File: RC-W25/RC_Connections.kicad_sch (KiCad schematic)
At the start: 23 parts, among them J1 USB_C_Receptacle_USB2.0_14P, U1 ESP32-C6-WROOM-1, U2 AP62300TWU

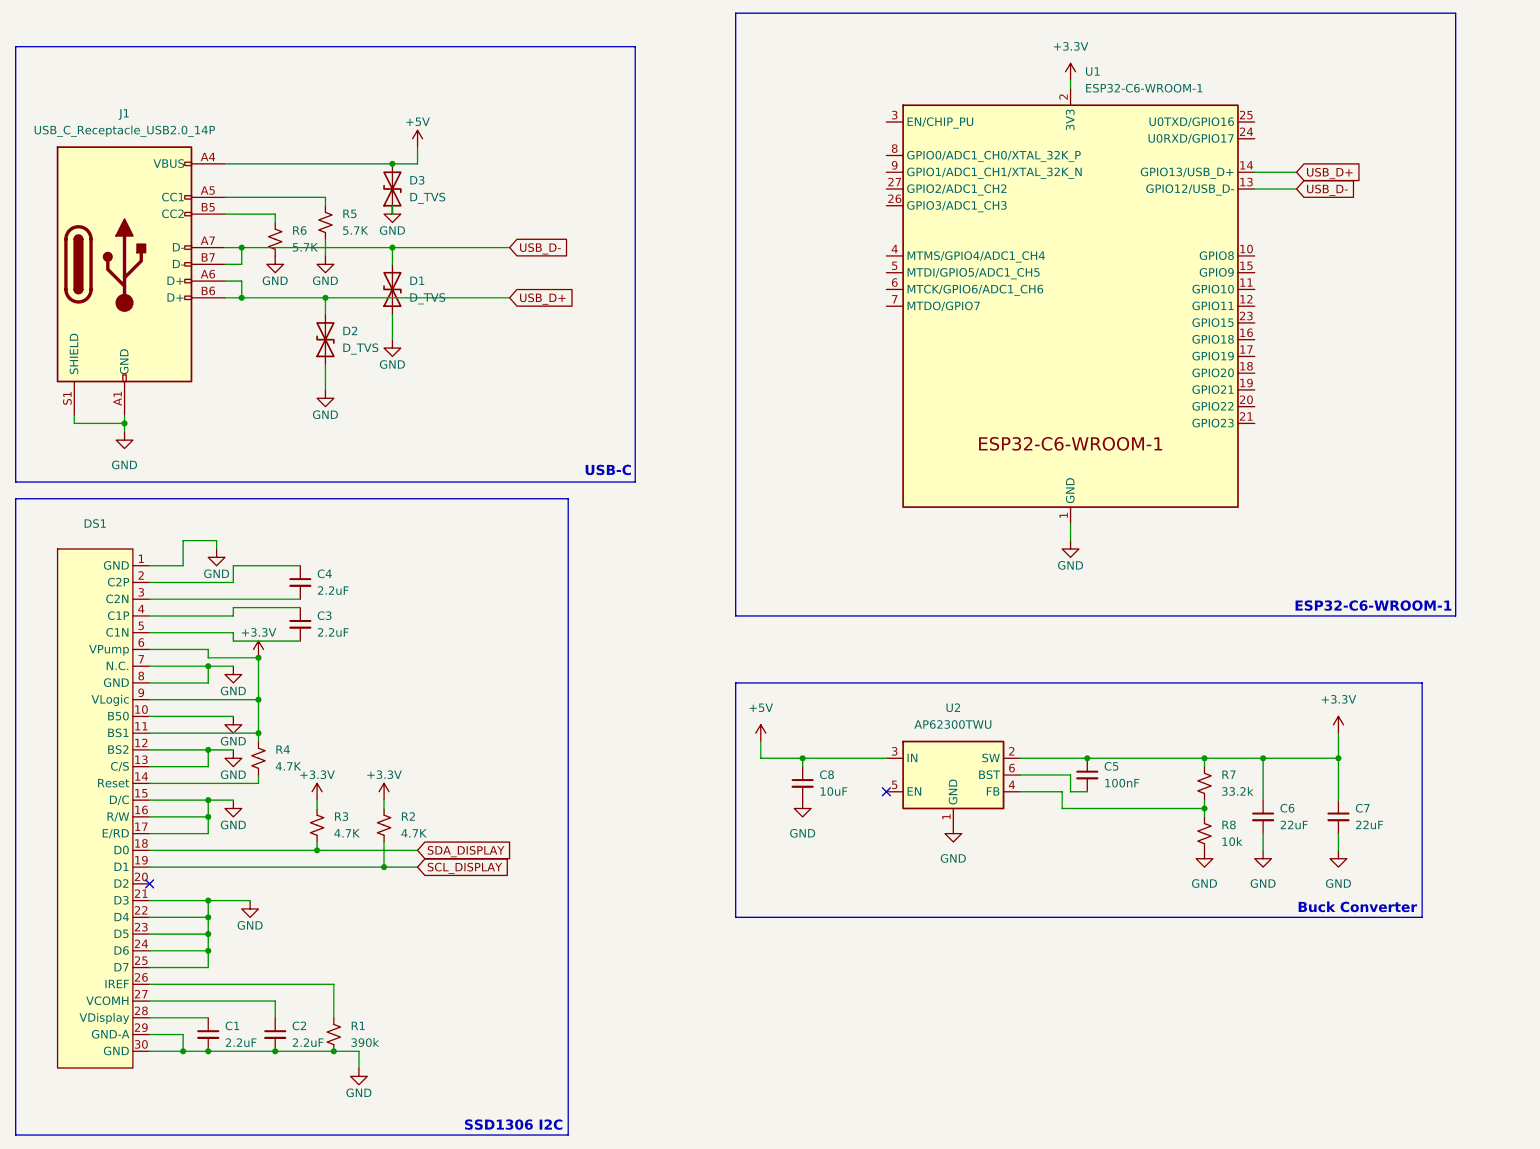
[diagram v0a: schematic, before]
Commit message: Schematic Update
Added buttons with debouncing and DC motor duraclik connector
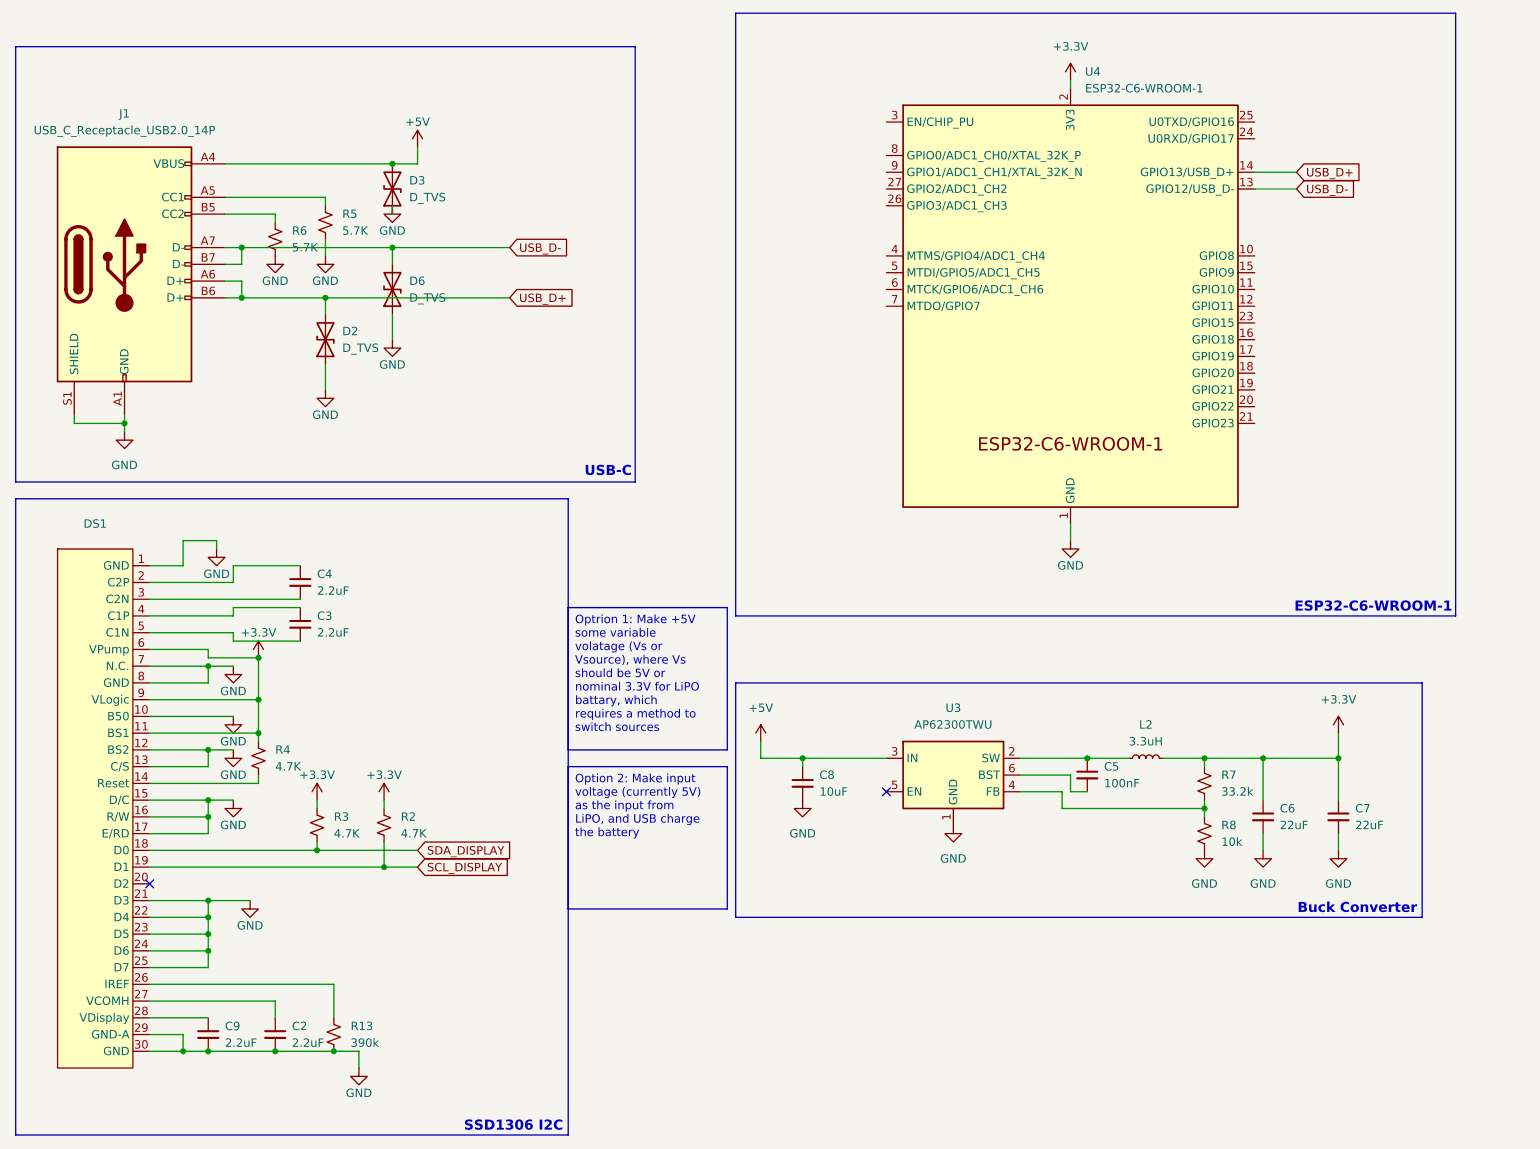
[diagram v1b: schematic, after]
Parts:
- added L2: 3.3uH, symbol Device:L_Small
- renumbered C1 to C9, D1 to D6, R1 to R13, U2 to U3, U1 to U4
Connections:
- net +3.3V: now also L2.2; no longer C5.1, U3.2 (SW)
- new net: C5.1, L2.1, U3.2 (SW)
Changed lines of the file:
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@@
 	(wire
 		(pts
+			(xy 207.01 133.35) (xy 213.36 133.35)
+		)
+		(stroke
+			(width 0)
+			(type default)
+		)
+	)
+	(wire
+		(pts
 			(xy 66.04 106.68) (xy 66.04 104.14)
 		)
@@
 	(wire
 		(pts
-			(xy 195.58 133.35) (xy 213.36 133.35)
+			(xy 195.58 133.35) (xy 201.93 133.35)
 		)
 		(stroke
@@
 		)
 	)
+	(text_box "Optrion 1: Make +5V some variable volatage (Vs or Vsource), where Vs should be 5V or nominal 3.3V for LiPO battary, which requires a method to switch sources"
+		(exclude_from_sim no)
+		(at 116.84 110.49 0)
+		(size 24.13 21.59)
+		(stroke
+			(width 0)
+			(type default)
+		)
+		(fill
+			(type none)
+		)
+		(effects
+			(font
+				(size 1.27 1.27)
+			)
+			(justify left top)
+		)
+	)
+	(text_box "Option 2: Make input voltage (currently 5V) as the input from LiPO, and USB charge the battery"
+		(exclude_from_sim no)
+		(at 116.84 134.62 0)
+		(size 24.13 21.59)
+		(stroke
+			(width 0)
+			(type default)
+		)
+		(fill
+			(type none)
+		)
+		(effects
+			(font
+				(size 1.27 1.27)
+			)
+			(justify left top)
+		)
+	)
 	(text "USB-C"
 		(exclude_from_sim no)
@@
 		(on_board yes)
 		(dnp no)
-		(property "Reference" "#PWR04"
+		(property "Reference" "#PWR036"
 			(at 78.74 143.51 0)
 			(effects
@@
 		(pin "1"
 		)
-		(instances
-			(project ""
-				(path "/427b2895-e3a6-4096-b101-5f65a3f7473e/01bd870e-4674-4257-9660-564635d632de"
-					(reference "#PWR04")
-					(unit 1)
-				)
-			)
-		)
 	)
 	(symbol
@@
 		(dnp no)
 		(fields_autoplaced yes)
-		(property "Reference" "U2"
+		(property "Reference" "U3"
 			(at 175.26 125.73 0)
 			(effects
@@
 		(pin "2"
 		)
-		(instances
-			(project ""
-				(path "/427b2895-e3a6-4096-b101-5f65a3f7473e/01bd870e-4674-4257-9660-564635d632de"
-					(reference "U2")
-					(unit 1)
-				)
-			)
-		)
 	)
 	(symbol
@@
 		(dnp no)
 		(fields_autoplaced yes)
-		(property "Reference" "#PWR021"
+		(property "Reference" "#PWR051"
 			(at 233.68 133.35 0)
 			(effects
@@
 		(pin "1"
 		)
-		(instances
-			(project ""
-				(path "/427b2895-e3a6-4096-b101-5f65a3f7473e/01bd870e-4674-4257-9660-564635d632de"
-					(reference "#PWR021")
-					(unit 1)
-				)
-			)
-		)
 	)
 	(symbol
@@
 		(on_board yes)
 		(dnp no)
-		(property "Reference" "#PWR026"
+		(property "Reference" "#PWR045"
 			(at 152.4 146.05 0)
 			(effects
@@
 		(pin "1"
 		)
-		(instances
-			(project ""
-				(path "/427b2895-e3a6-4096-b101-5f65a3f7473e/01bd870e-4674-4257-9660-564635d632de"
-					(reference "#PWR026")
-					(unit 1)
-				)
-			)
-		)
 	)
 	(symbol
@@
 		(dnp no)
 		(fields_autoplaced yes)
-		(property "Reference" "D1"
+		(property "Reference" "D6"
 			(at 92.71 60.9599 90)
 			(effects
@@
 		(pin "2"
 		)
-		(instances
-			(project ""
-				(path "/427b2895-e3a6-4096-b101-5f65a3f7473e/01bd870e-4674-4257-9660-564635d632de"
-					(reference "D1")
-					(unit 1)
-				)
-			)
-		)
 	)
 	(symbol
@@
 		(on_board yes)
 		(dnp no)
-		(property "Reference" "#PWR03"
+		(property "Reference" "#PWR033"
 			(at 68.58 161.29 0)
 			(effects
@@
 		(pin "1"
 		)
-		(instances
-			(project ""
-				(path "/427b2895-e3a6-4096-b101-5f65a3f7473e/01bd870e-4674-4257-9660-564635d632de"
-					(reference "#PWR03")
-					(unit 1)
-				)
-			)
-		)
 	)
 	(symbol
@@
 		(on_board yes)
 		(dnp no)
-		(property "Reference" "#PWR015"
+		(property "Reference" "#PWR043"
 			(at 93.98 44.45 0)
 			(effects
@@
 		(pin "1"
 		)
-		(instances
-			(project ""
-				(path "/427b2895-e3a6-4096-b101-5f65a3f7473e/01bd870e-4674-4257-9660-564635d632de"
-					(reference "#PWR015")
-					(unit 1)
-				)
-			)
-		)
 	)
 	(symbol
@@
 		(dnp no)
 		(fields_autoplaced yes)
-		(property "Reference" "#PWR020"
+		(property "Reference" "#PWR046"
 			(at 175.26 149.86 0)
 			(effects
@@
 		(pin "1"
 		)
-		(instances
-			(project ""
-				(path "/427b2895-e3a6-4096-b101-5f65a3f7473e/01bd870e-4674-4257-9660-564635d632de"
-					(reference "#PWR020")
-					(unit 1)
-				)
-			)
-		)
 	)
 	(symbol
@@
 		(dnp no)
 		(fields_autoplaced yes)
-		(property "Reference" "U1"
+		(property "Reference" "U4"
 			(at 195.2341 29.21 0)
 			(effects
@@
 		(pin "9"
 		)
-		(instances
-			(project ""
-				(path "/427b2895-e3a6-4096-b101-5f65a3f7473e/01bd870e-4674-4257-9660-564635d632de"
-					(reference "U1")
-					(unit 1)
-				)
-			)
-		)
 	)
 	(symbol
@@
 		(dnp no)
 		(fields_autoplaced yes)
-		(property "Reference" "R1"
+		(property "Reference" "R13"
 			(at 83.82 173.9899 0)
 			(effects
@@
 		(pin "2"
 		)
-		(instances
-			(project ""
-				(path "/427b2895-e3a6-4096-b101-5f65a3f7473e/01bd870e-4674-4257-9660-564635d632de"
-					(reference "R1")
-					(unit 1)
-				)
-			)
-		)
 	)
 	(symbol
@@
 		(dnp no)
 		(fields_autoplaced yes)
-		(property "Reference" "#PWR025"
+		(property "Reference" "#PWR044"
 			(at 146.05 134.62 0)
 			(effects
@@
 		(pin "1"
 		)
-		(instances
-			(project ""
-				(path "/427b2895-e3a6-4096-b101-5f65a3f7473e/01bd870e-4674-4257-9660-564635d632de"
-					(reference "#PWR025")
-					(unit 1)
-				)
-			)
-		)
 	)
 	(symbol
@@
 		(dnp no)
 		(fields_autoplaced yes)
-		(property "Reference" "#PWR019"
+		(property "Reference" "#PWR047"
 			(at 193.04 34.29 0)
 			(effects
@@
 		(pin "1"
 		)
-		(instances
-			(project ""
-				(path "/427b2895-e3a6-4096-b101-5f65a3f7473e/01bd870e-4674-4257-9660-564635d632de"
-					(reference "#PWR019")
-					(unit 1)
-				)
-			)
-		)
 	)
 	(symbol
@@
 	)
 	(symbol
+		(lib_id "Device:L_Small")
+		(at 204.47 133.35 90)
+		(unit 1)
+		(exclude_from_sim no)
+		(in_bom yes)
+		(on_board yes)
+		(dnp no)
+		(fields_autoplaced yes)
+		(property "Reference" "L2"
+			(at 204.47 128.27 90)
+			(effects
+				(font
+					(size 1.27 1.27)
+				)
+			)
+		)
+		(property "Value" "3.3uH"
+			(at 204.47 130.81 90)
+			(effects
+				(font
+					(size 1.27 1.27)
+				)
+			)
+		)
+		(property "Footprint" ""
+			(at 204.47 133.35 0)
+			(effects
+				(font
+					(size 1.27 1.27)
+				)
+				(hide yes)
+			)
+		)
+		(property "Datasheet" "~"
+			(at 204.47 133.35 0)
+			(effects
+				(font
+					(size 1.27 1.27)
+				)
+				(hide yes)
+			)
+		)
+		(property "Description" "Inductor, small symbol"
+			(at 204.47 133.35 0)
+			(effects
+				(font
+					(size 1.27 1.27)
+				)
+				(hide yes)
+			)
+		)
+		(pin "1"
+		)
+		(pin "2"
+		)
+	)
+	(symbol
 		(lib_id "power:GND")
 		(at 49.53 83.82 0)
@@
 		(dnp no)
 		(fields_autoplaced yes)
-		(property "Reference" "#PWR01"
+		(property "Reference" "#PWR027"
 			(at 49.53 90.17 0)
 			(effects
@@
 		(pin "1"
 		)
-		(instances
-			(project ""
-				(path "/427b2895-e3a6-4096-b101-5f65a3f7473e/01bd870e-4674-4257-9660-564635d632de"
-					(reference "#PWR01")
-					(unit 1)
-				)
-			)
-		)
 	)
 	(symbol
@@
 		(dnp no)
 		(fields_autoplaced yes)
-		(property "Reference" "#PWR022"
+		(property "Reference" "#PWR049"
 			(at 213.36 153.67 0)
 			(effects
@@
 		(pin "1"
 		)
-		(instances
-			(project ""
-				(path "/427b2895-e3a6-4096-b101-5f65a3f7473e/01bd870e-4674-4257-9660-564635d632de"
-					(reference "#PWR022")
-					(unit 1)
-				)
-			)
-		)
 	)
 	(symbol
@@
 		(dnp no)
 		(fields_autoplaced yes)
-		(property "Reference" "C1"
+		(property "Reference" "C9"
 			(at 64.77 173.9962 0)
 			(effects
@@
 		(pin "1"
 		)
-		(instances
-			(project ""
-				(path "/427b2895-e3a6-4096-b101-5f65a3f7473e/01bd870e-4674-4257-9660-564635d632de"
-					(reference "C1")
-					(unit 1)
-				)
-			)
-		)
 	)
 	(symbol
@@
 		(on_board yes)
 		(dnp no)
-		(property "Reference" "#PWR02"
+		(property "Reference" "#PWR039"
 			(at 85.09 186.69 0)
 			(effects
@@
 		(pin "1"
 		)
-		(instances
-			(project ""
-				(path "/427b2895-e3a6-4096-b101-5f65a3f7473e/01bd870e-4674-4257-9660-564635d632de"
-					(reference "#PWR02")
-					(unit 1)
-				)
-			)
-		)
 	)

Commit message: Updated Schematic
Introduced linear hall effect sensors
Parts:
- added C11, C13: 100nF, Capacitor_SMD:C_0603_1608Metric, symbol Device:C_Small
- renumbered C9 to C?, D6 to D?, L2 to L?, R13 to R?, U4 to U1, U3 to U2
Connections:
- net GND: now also C11.2, C13.2
- net GPIO_EN1: now reaches U1.10 (GPIO8)
- net GPIO_PWR: now reaches U1.11 (GPIO10)
- net GPIO_MODE: now reaches U1.12 (GPIO11)
- net GPIO_EN2: now reaches U1.15 (GPIO9)
- net ADC_HALLEFFECT1: now reaches U1.8 (GPIO0/ADC1_CH0/XTAL_32K_P)
- net ADC_HALLEFFECT1: now also C13.1
- net ADC_HALLEFFECT2: now reaches U1.9 (GPIO1/ADC1_CH1/XTAL_32K_N)
- net ADC_HALLEFFECT2: now also C11.1
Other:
- note added: "**replace later for switch"
- note added: "ADC Input Decaps"
- note added: "Differential Routing"
- moved on the sheet: C5, C6, C7, C8, L?, R7, R8, U2
